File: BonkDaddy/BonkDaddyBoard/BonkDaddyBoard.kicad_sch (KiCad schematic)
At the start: 45 parts, among them J1 EXP, J2 USB_B_Micro, J3 USB_A, Q3 2N7000, Q4 2N3906, SW1 Reset, U1 74AHC04

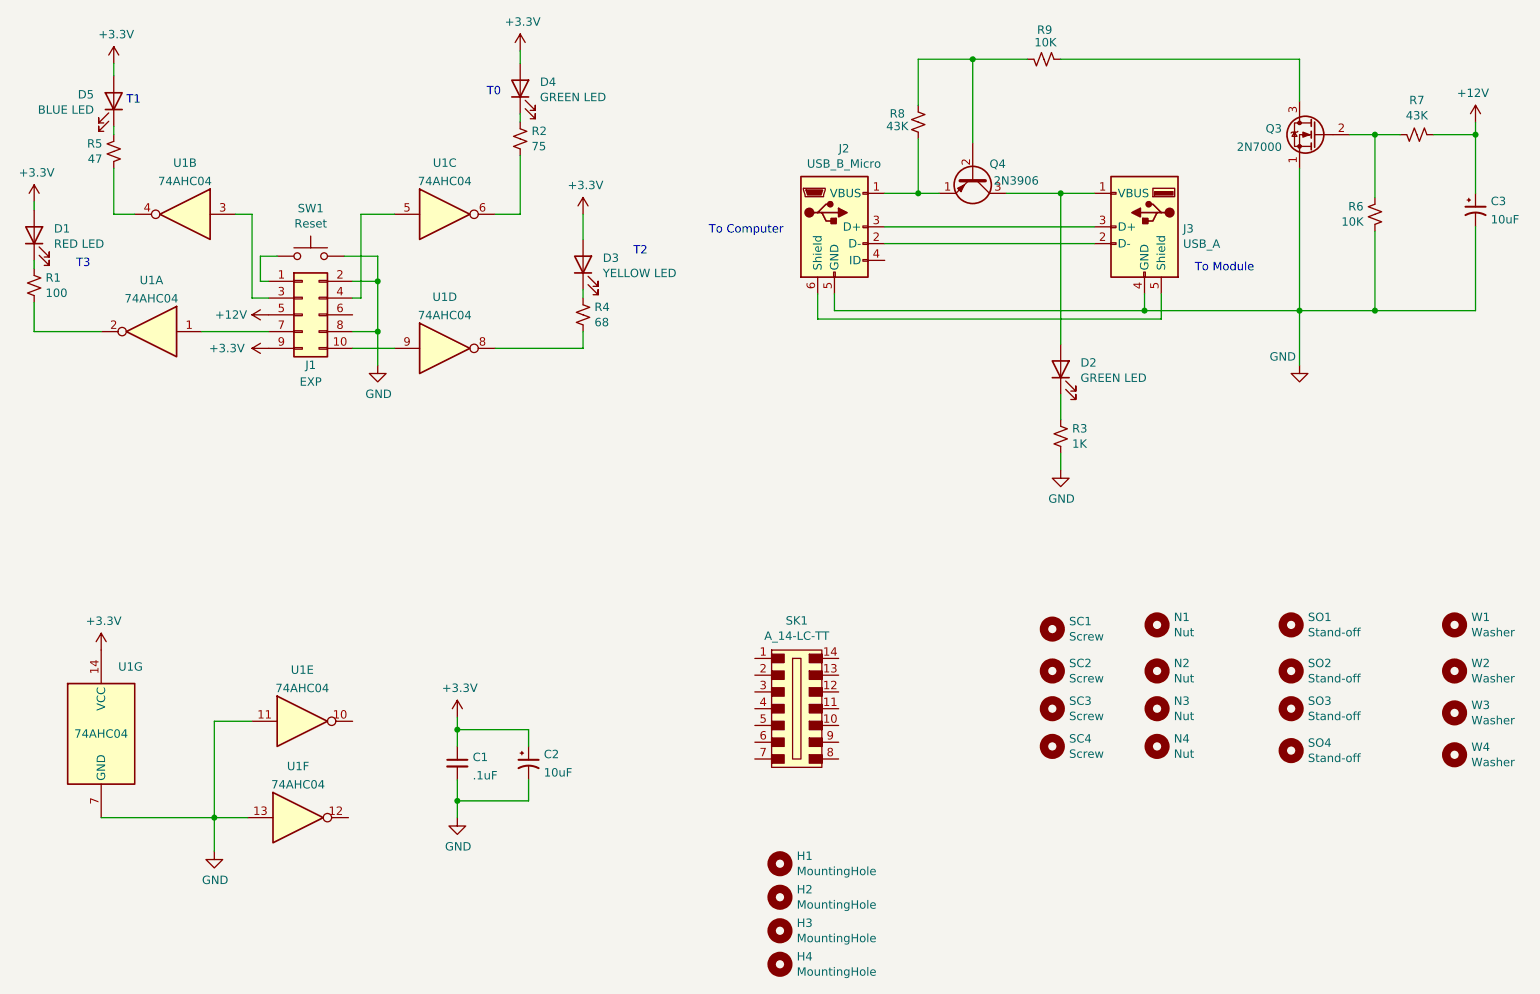
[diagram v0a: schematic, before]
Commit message: Updated LED resistors
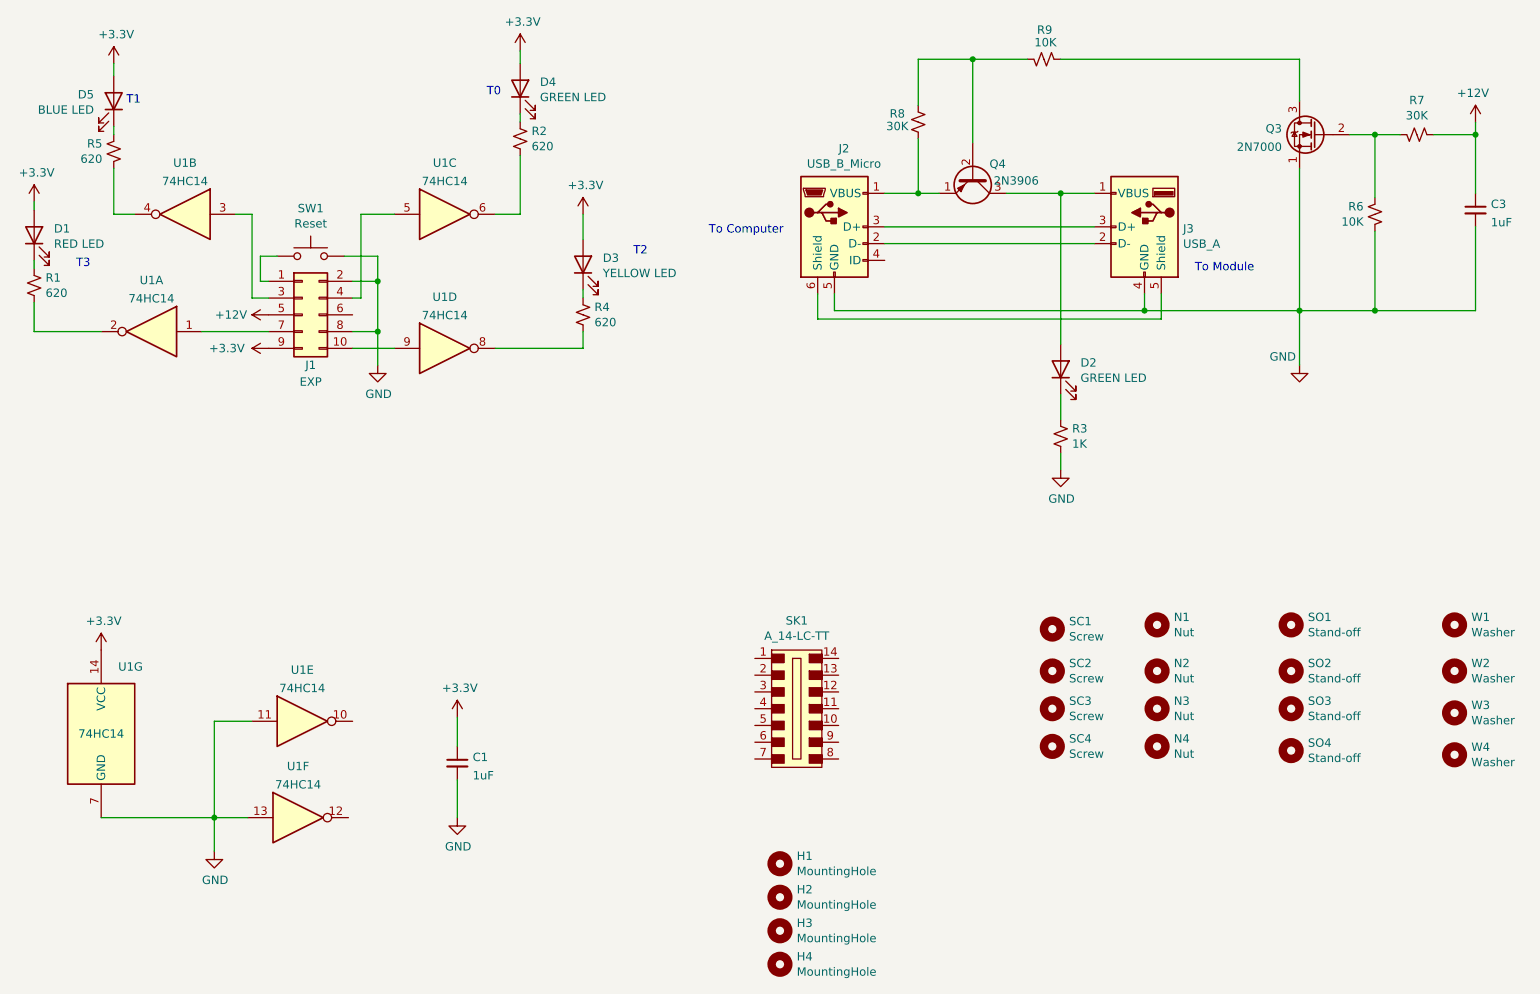
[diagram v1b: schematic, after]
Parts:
- removed C2, C3: 10uF, Capacitor_THT:CP_Radial_D5.0mm_P2.00mm, symbol Device:C_Polarized_Small_US
- added C3: 1uF, Capacitor_THT:C_Rect_L7.0mm_W2.0mm_P5.00mm, symbol Device:C_Small
- C1: value .1uF -> 1uF; Digi-Key Part 399-9877-2-ND -> 399-9886-1-ND; LCSC Part # (none) -> C94708
- J1: LCSC Part # (none) -> C225520
- J3: LCSC Part # (none) -> C386737
- Q3: Digi-Key Part 2N7000BU-ND -> 2N7000FS-ND; LCSC Part # (none) -> C232838
- Q4: LCSC Part # (none) -> C9809
- R1: value 100 -> 620; Digi-Key Part CF14JT100RCT-ND -> CF14JT620RCT-ND; LCSC Part # (none) -> C120050
- R2: value 75 -> 620; Digi-Key Part CF14JT75R0CT-ND -> CF14JT620RCT-ND; LCSC Part # (none) -> C120050
- R3: Digi-Key Part 738-CFF14JT1K00CT-ND -> CF14JT1K00CT-ND; LCSC Part # (none) -> C120055
- R4: value 68 -> 620; Digi-Key Part CF14JT68R0CT-ND -> CF14JT620RCT-ND; LCSC Part # (none) -> C120050
- R5: value 47 -> 620; Digi-Key Part CF14JT47R0CT-ND -> CF14JT620RCT-ND; LCSC Part # (none) -> C120050
- R6, R9: LCSC Part # (none) -> C433778
- R7: value 43K -> 30K; footprint Resistor_THT:R_Axial_DIN0207_L6.3mm_D2.5mm_P10.16mm_Horizontal -> Resistor_THT:R_Axial_DIN0207_L6.3mm_D2.5mm_P2.54mm_Vertical; Digi-Key Part CF14JT43K0CT-ND -> CF14JT30K0CT-ND; LCSC Part # (none) -> C176499
- R8: value 43K -> 30K; Digi-Key Part CF14JT43K0CT-ND -> CF14JT30K0CT-ND; LCSC Part # (none) -> C176499
- SK1: footprint (none) -> Package_DIP:DIP-14_W7.62mm_Socket; LCSC Part # (none) -> C132508
- U1: value 74AHC04 -> 74HC14; Digi-Key Part 296-12772-5-ND -> TC74HC14APF-ND
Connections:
- net +12V: now also C3.1
- net GND: now also C3.2
